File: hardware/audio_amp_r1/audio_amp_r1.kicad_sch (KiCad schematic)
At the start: 15 parts, among them J1 AudioJack4, J2 AudioJack4, J3 Conn_01x02, J4 Conn_01x04_Pin, J5 Conn_01x04_Pin, U1 AD8397

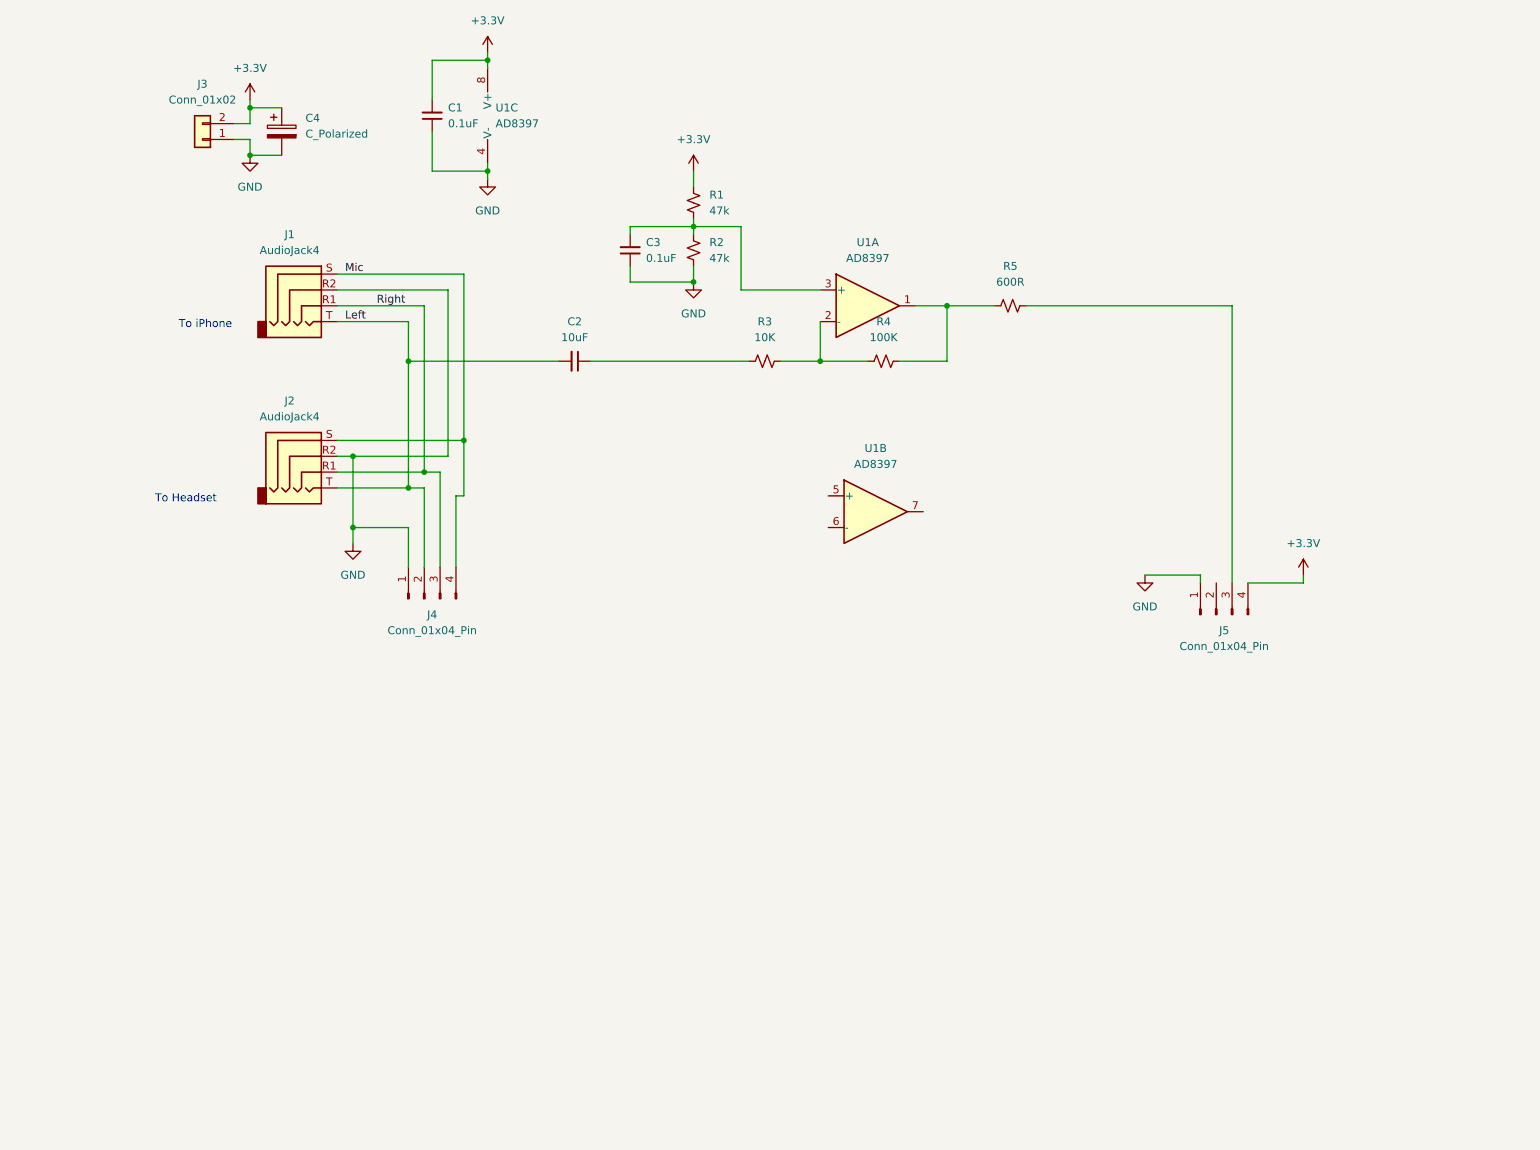
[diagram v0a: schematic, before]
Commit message: start updates for BNC connectors
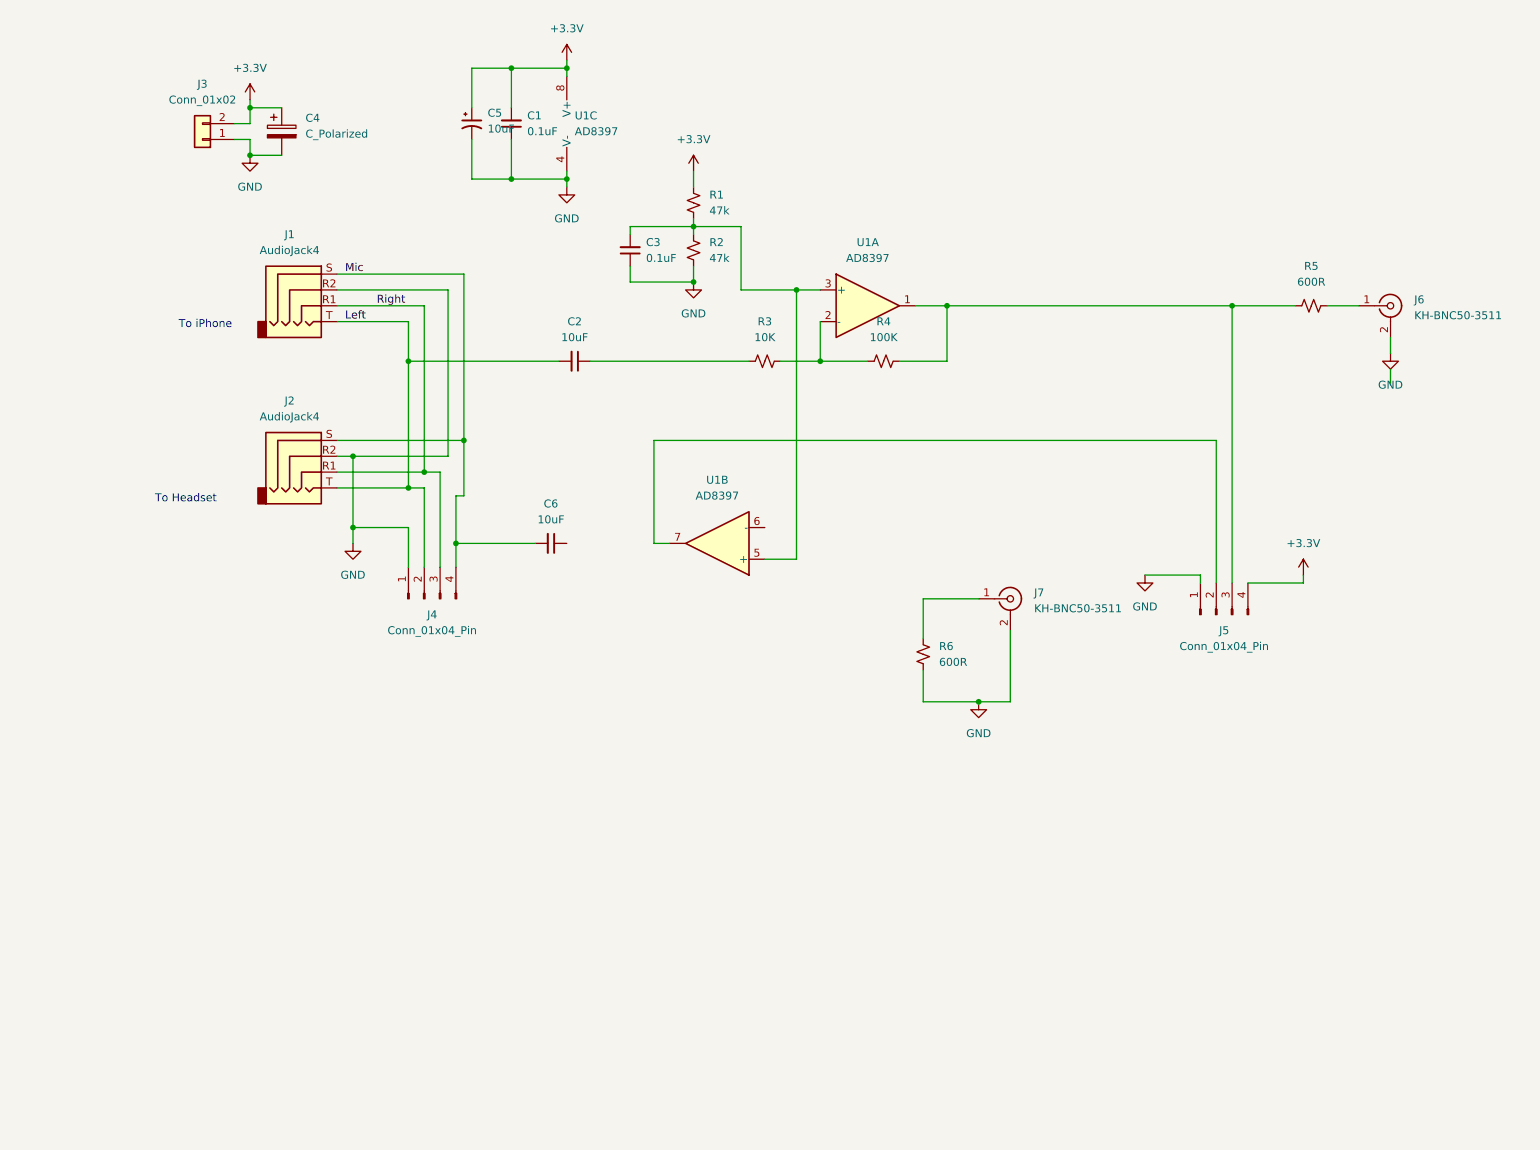
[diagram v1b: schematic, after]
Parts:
- added C5: 10uF, Capacitor_Tantalum_SMD:CP_EIA-3216-12_Kemet-S, symbol Device:C_Polarized_Small_US
- added C6: 10uF, Capacitor_SMD:C_1206_3216Metric, symbol Device:C_Small
- added J6, J7: KH-BNC50-3511, Connector_Coaxial:BNC_Amphenol_B6252HB-NPP3G-50_Horizontal, symbol Connector:Conn_Coaxial
- added R6: 600R, Resistor_SMD:R_0805_2012Metric, symbol Device:R_Small_US
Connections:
- net +3.3V: now also C5.1
- net GND: now also C5.2, J6.2 (Ext), J7.2 (Ext), R6.2
- net Mic: now also C6.2
- net at R4.1, R5.2, U1.1: now also J5.3 (Pin_3)
- net at J5.2 (Pin_2): now also U1.7
- net at R5.1: now also J6.1 (In); no longer J5.3 (Pin_3)
- net at U1.5 (+): now also C3.2, R1.1, R2.2, U1.3 (+)
- new net: J7.1 (In), R6.1
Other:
- moved on the sheet: C1, R5, U1B, U1C

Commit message: update parts numbers and footprints
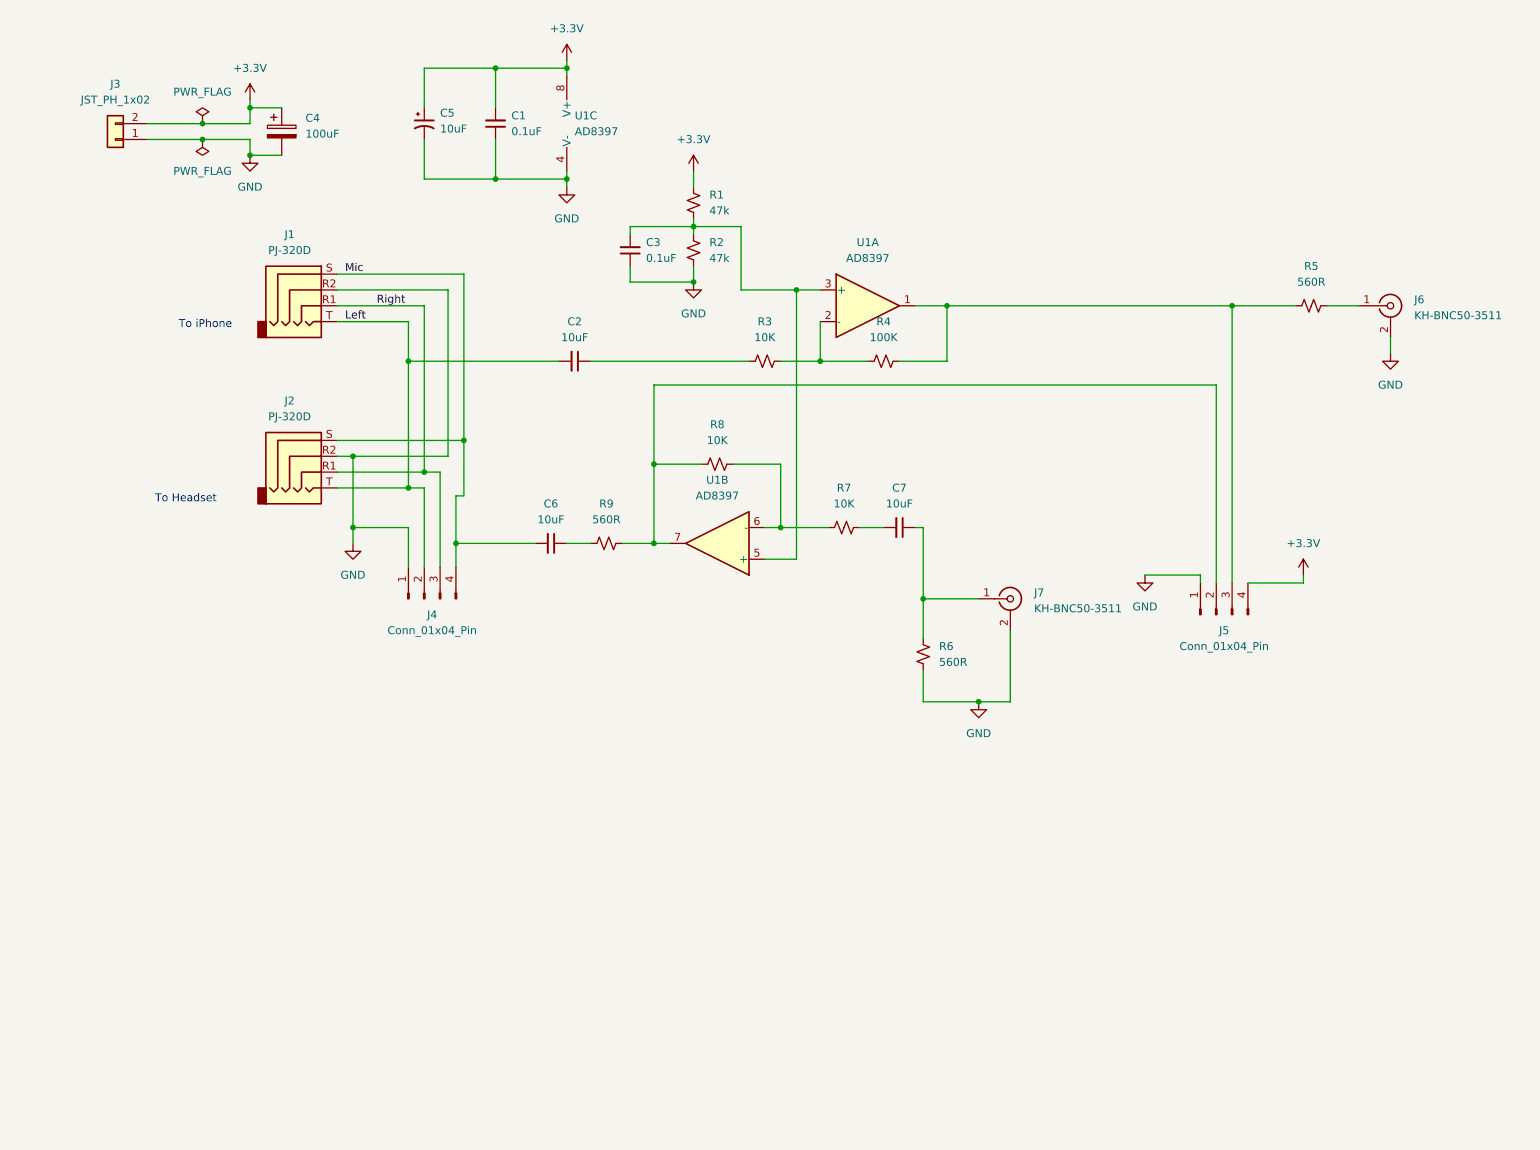
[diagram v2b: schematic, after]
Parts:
- added C7: 10uF, Capacitor_SMD:C_0805_2012Metric, symbol Device:C_Small
- added R7, R8: 10K, Resistor_SMD:R_0805_2012Metric, symbol Device:R_Small_US
- added R9: 560R, Resistor_SMD:R_0805_2012Metric, symbol Device:R_Small_US
- C1, C3: footprint Capacitor_SMD:C_0603_1608Metric -> Capacitor_SMD:C_0805_2012Metric; JLCPCB Part # (none) -> C49678
- C2, C6: footprint Capacitor_SMD:C_1206_3216Metric -> Capacitor_SMD:C_0805_2012Metric; JLCPCB Part # (none) -> C15850
- C4: value C_Polarized -> 100uF; footprint Capacitor_Tantalum_SMD:CP_EIA-2012-12_Kemet-R -> Capacitor_Tantalum_SMD:CP_EIA-3528-21_Kemet-B; JLCPCB Part # (none) -> C16133
- C5: footprint Capacitor_Tantalum_SMD:CP_EIA-3216-12_Kemet-S -> Capacitor_Tantalum_SMD:CP_EIA-3216-18_Kemet-A; JLCPCB Part # (none) -> C7171
- J1, J2: value AudioJack4 -> PJ-320D; JLCPCB Part # (none) -> C431535; MPN (none) -> PJ-320D
- J3: value Conn_01x02 -> JST_PH_1x02; footprint Connector_PinHeader_2.54mm:PinHeader_1x02_P2.54mm_Vertical -> Connector_JST:JST_PH_S2B-PH-SM4-TB_1x02-1MP_P2.00mm_Horizontal; JLCPCB Part # (none) -> C295747
- J4, J5: footprint Connector_PinHeader_2.54mm:PinHeader_1x04_P2.54mm_Vertical -> Connector_PinHeader_2.54mm:PinHeader_1x04_P2.54mm_Vertical_SMD_Pin1Left; JLCPCB Part # (none) -> C2881610
- R1, R2: footprint Resistor_SMD:R_0603_1608Metric -> Resistor_SMD:R_0805_2012Metric; JLCPCB Part # (none) -> C17713
- R3: JLCPCB Part # (none) -> C17414
- R4: JLCPCB Part # (none) -> C149504
- R5, R6: value 600R -> 560R; JLCPCB Part # (none) -> C28636
- U1: JLCPCB Part # (none) -> C578714
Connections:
- net at C6.1: now also R9.1
- net at J7.1 (In), R6.1: now also C7.1
- net at J5.2 (Pin_2), U1.7: now also R8.2, R9.2
- net at U1.6 (-): now also R7.2, R8.1
- new net: C7.2, R7.1
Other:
- moved on the sheet: C1, C5, J3

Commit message: fix up rotations for JLCPCB
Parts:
- J1, J2, J4, J5: JLCPCB Rotation Offset (none) -> 90
- J6, J7: JLCPCB Rotation Offset 0 -> 180
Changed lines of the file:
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@@
       (effects (font (size 1.27 1.27)) hide)
     )
-    (property "JLCPCB Rotation Offset" "0" (at 186.69 107.95 0)
+    (property "JLCPCB Rotation Offset" "180" (at 186.69 107.95 0)
       (effects (font (size 1.27 1.27)) hide)
     )
@@
     )
     (property "JLCPCB Part #" "C2881610" (at 219.71 110.49 0)
+      (effects (font (size 1.27 1.27)) hide)
+    )
+    (property "JLCPCB Rotation Offset" "90" (at 219.71 110.49 0)
       (effects (font (size 1.27 1.27)) hide)
     )
@@
       (effects (font (size 1.27 1.27)) hide)
     )
-    (property "JLCPCB Rotation Offset" "0" (at 247.65 60.96 0)
+    (property "JLCPCB Rotation Offset" "180" (at 247.65 60.96 0)
       (effects (font (size 1.27 1.27)) hide)
     )
@@
       (effects (font (size 1.27 1.27)) hide)
     )
+    (property "JLCPCB Rotation Offset" "90" (at 73.66 58.42 0)
+      (effects (font (size 1.27 1.27)) hide)
+    )
     (pin "R1")
     (pin "R2")
@@
       (effects (font (size 1.27 1.27)) hide)
     )
+    (property "JLCPCB Rotation Offset" "90" (at 73.66 85.09 0)
+      (effects (font (size 1.27 1.27)) hide)
+    )
     (pin "R1")
     (pin "R2")
@@
       (effects (font (size 1.27 1.27)) hide)
     )
+    (property "JLCPCB Rotation Offset" "90" (at 92.71 107.95 0)
+      (effects (font (size 1.27 1.27)) hide)
+    )
